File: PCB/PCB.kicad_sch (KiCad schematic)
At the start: 21 parts, among them J1 Conn_01x06_Female, U13 74HC165, U15 LT3042xMSE, U16 74HC165

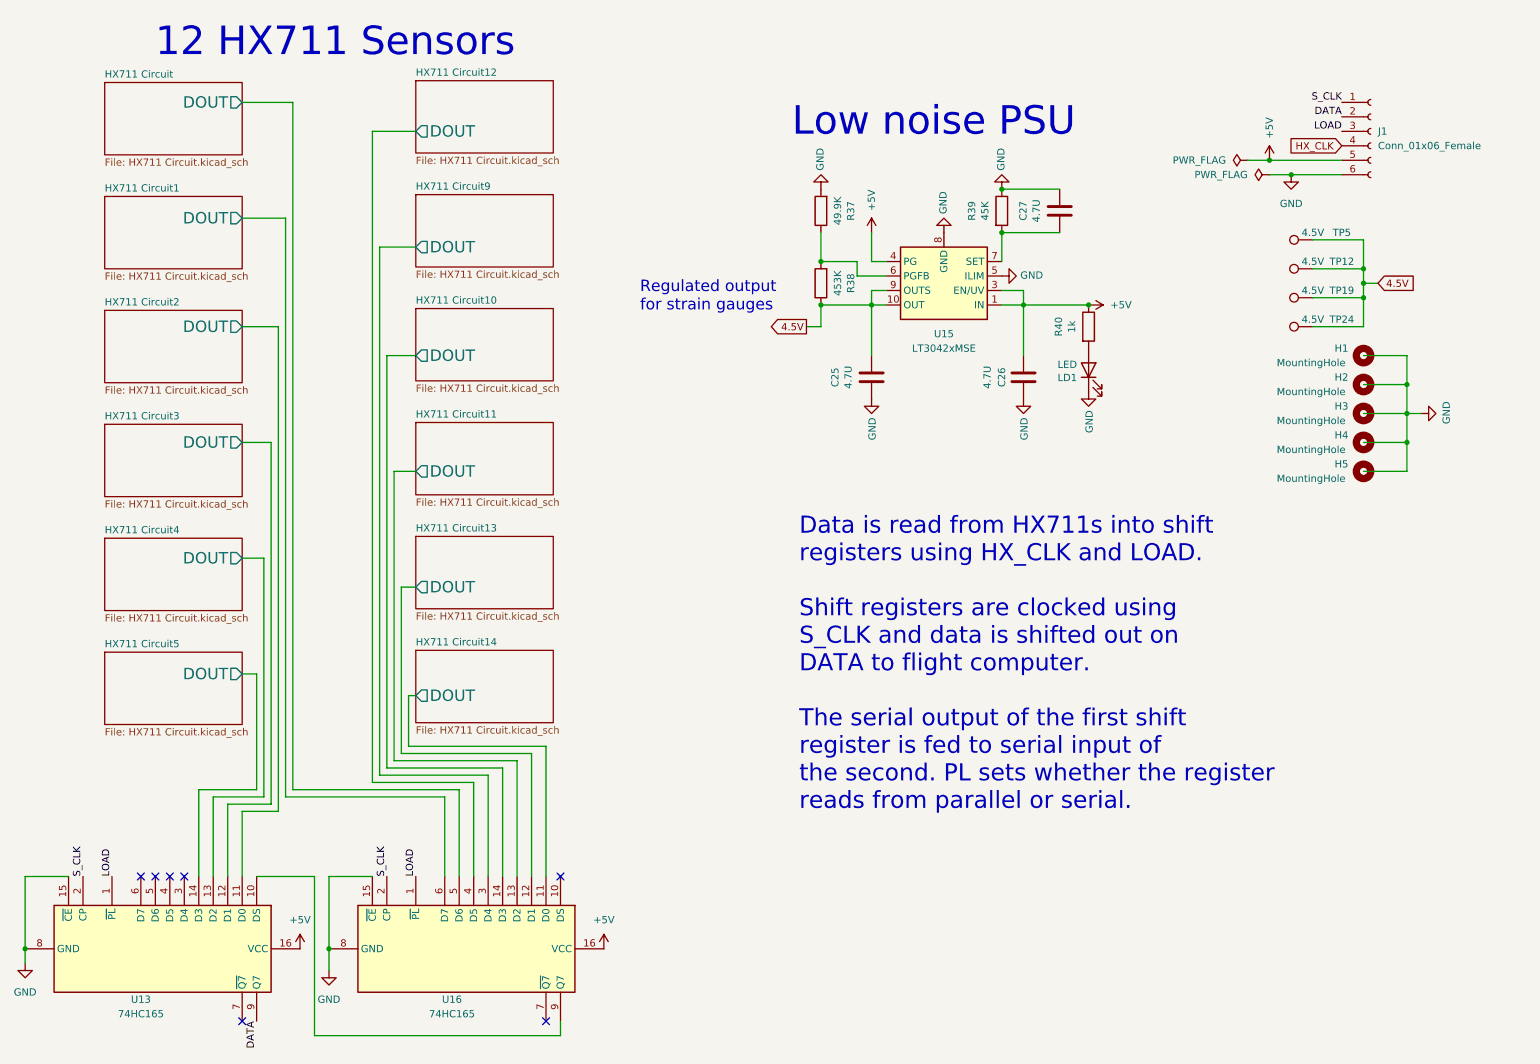
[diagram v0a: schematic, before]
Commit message: Switch VDD to 3.3V. Ready for comp
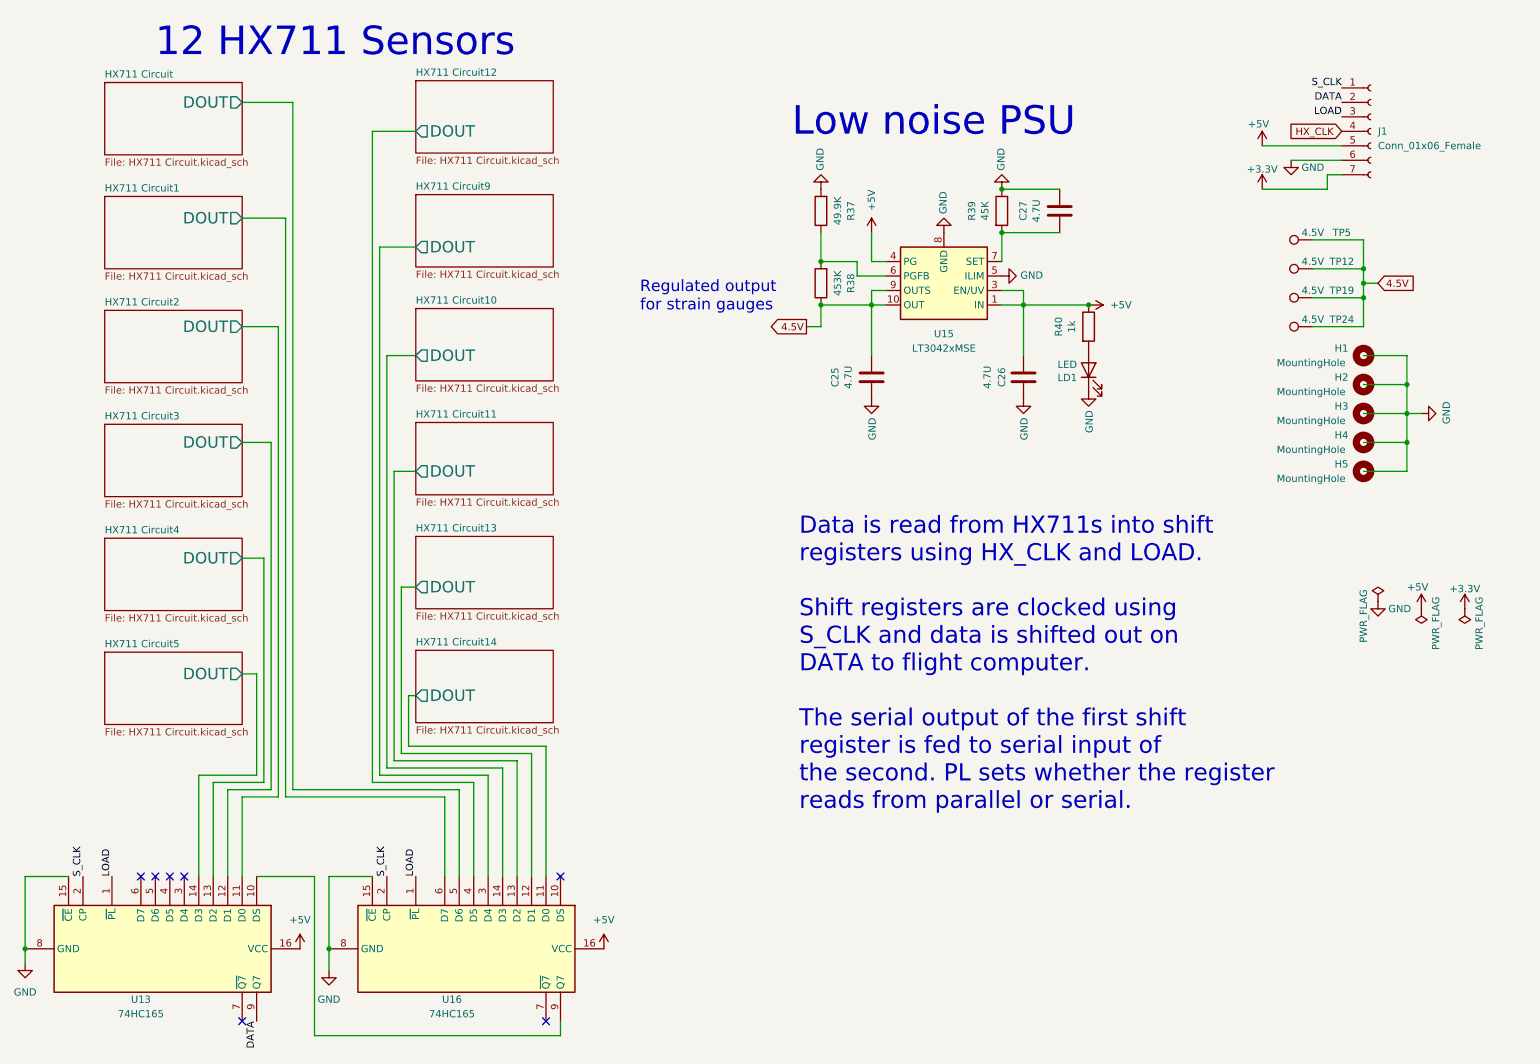
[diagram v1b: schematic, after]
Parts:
- J1: footprint Connector_JST:JST_EH_B6B-EH-A_1x06_P2.50mm_Vertical -> Connector_JST:JST_XH_B7B-XH-A_1x07_P2.50mm_Vertical; symbol Connector:Conn_01x06_Female -> Connector:Conn_01x07_Socket
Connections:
- new net +3.3V: J1.7 (Pin_7)

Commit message: Found connector
Found connector, kicad layout and everything else I needed.
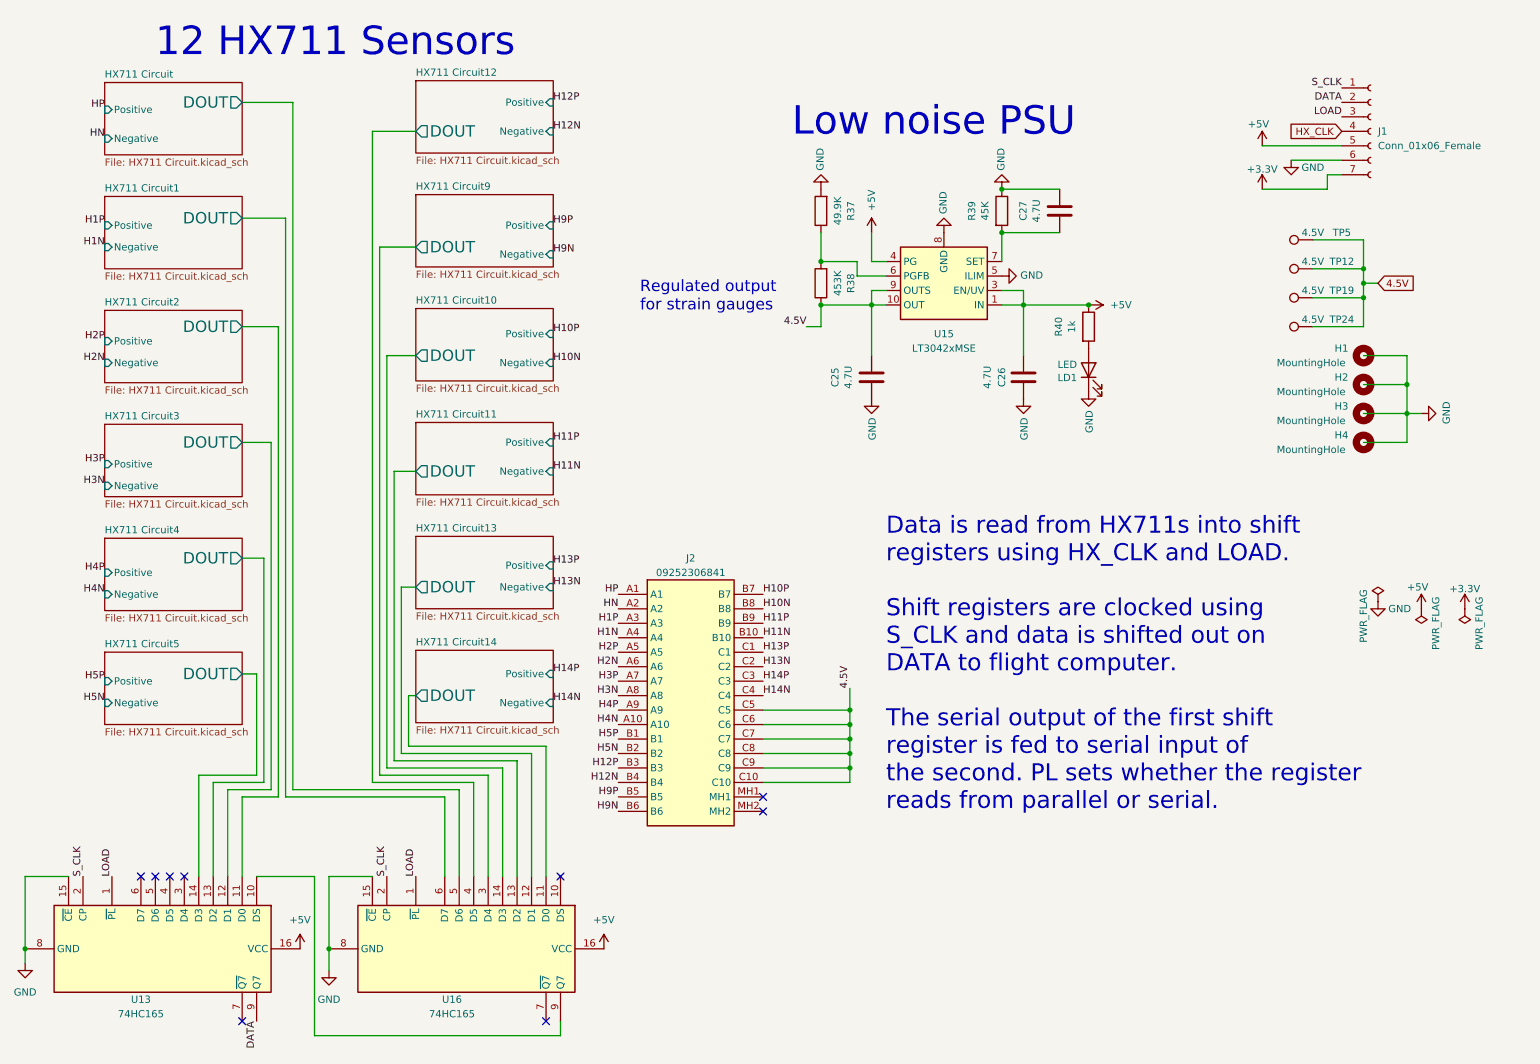
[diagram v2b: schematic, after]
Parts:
- removed H5: MountingHole, MountingHole:MountingHole_6.4mm_M6_Pad_TopBottom, symbol Mechanical:MountingHole
- added J2: 09252306841, 09252306841:09252306841, symbol 09252306841:09252306841
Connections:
- net 4.5V: now also J2.C10, J2.C5, J2.C6, J2.C7, J2.C8, J2.C9
- new net H10N: J2.B8
- new net H10P: J2.B7
- new net H11N: J2.B10
- new net H11P: J2.B9
- new net H12N: J2.B4
- new net H12P: J2.B3
- new net H13N: J2.C2
- new net H13P: J2.C1
- new net H14N: J2.C4
- new net H14P: J2.C3
- new net H1N: J2.A4
- new net H1P: J2.A3
- new net H2N: J2.A6
- new net H2P: J2.A5
- new net H3N: J2.A8
- new net H3P: J2.A7
- new net H4N: J2.A10
- new net H4P: J2.A9
- new net H5N: J2.B2
- new net H5P: J2.B1
- new net H9N: J2.B6
- new net H9P: J2.B5
- new net HN: J2.A2
- new net HP: J2.A1
- no-connect marks 7 -> 9
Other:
- sheet HX711 Circuit ports: added Negative, Positive; removed none
- sheet HX711 Circuit1 ports: added Negative, Positive; removed none
- sheet HX711 Circuit10 ports: added Negative, Positive; removed none
- sheet HX711 Circuit11 ports: added Negative, Positive; removed none
- sheet HX711 Circuit12 ports: added Negative, Positive; removed none
- sheet HX711 Circuit13 ports: added Negative, Positive; removed none
- sheet HX711 Circuit14 ports: added Negative, Positive; removed none
- sheet HX711 Circuit2 ports: added Negative, Positive; removed none
- sheet HX711 Circuit3 ports: added Negative, Positive; removed none
- sheet HX711 Circuit4 ports: added Negative, Positive; removed none
- sheet HX711 Circuit5 ports: added Negative, Positive; removed none
- sheet HX711 Circuit9 ports: added Negative, Positive; removed none
